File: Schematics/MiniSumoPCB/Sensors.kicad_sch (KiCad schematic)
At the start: 15 parts, among them J10 TOF_L, J11 TOF_R, J12 EXTRA_I2C1, J12 EXTRA_I2C2, J12 TOF_B, J7 Line_L, J7 TOF_F, J8 TOF_FR, J9 Line_R, J9 TOF_FL, U4 TCA9548APWR

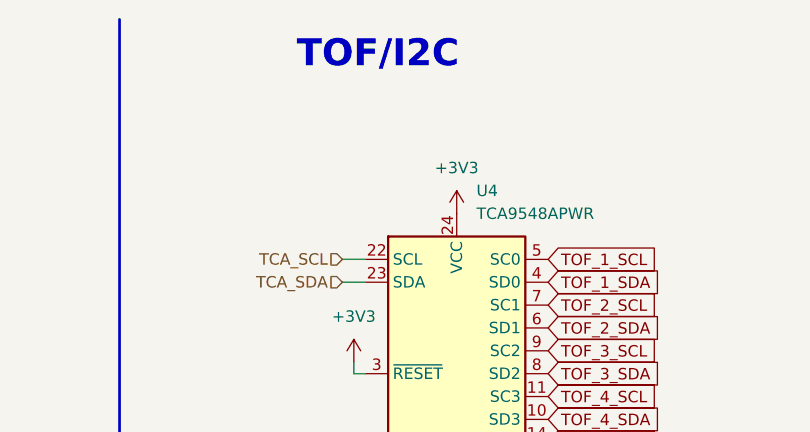
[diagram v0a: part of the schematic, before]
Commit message: [PCB] Added decoupling Capacitors
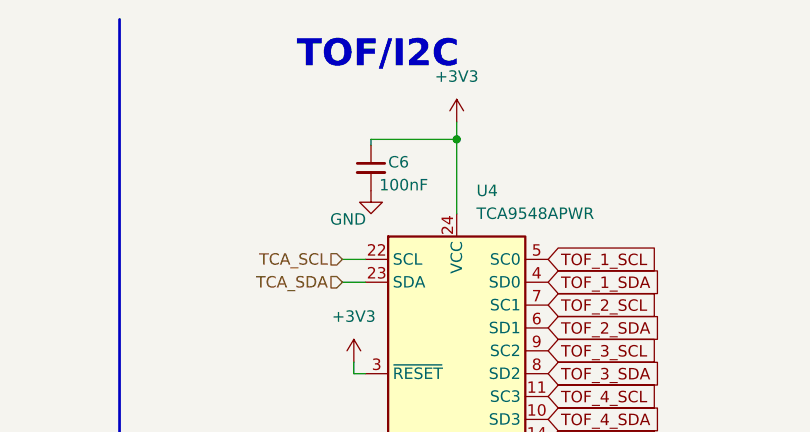
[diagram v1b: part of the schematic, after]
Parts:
- added C6: 100nF, Capacitor_SMD:C_1206_3216Metric_Pad1.33x1.80mm_HandSolder, symbol Device:C_Small
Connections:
- net +3V3: now also C6.1
- net GND: now also C6.2
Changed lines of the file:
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@@
   (junction (at 55.245 102.235) (diameter 0) (color 0 0 0 0)
   )
+  (junction (at 187.96 26.035) (diameter 0) (color 0 0 0 0)
+  )
   (wire (pts (xy 55.245 89.535) (xy 59.055 89.535))
     (stroke (width 0) (type default))
@@
     (stroke (width 0) (type default))
   )
+  (wire (pts (xy 178.435 26.67) (xy 178.435 26.035))
+    (stroke (width 0) (type default))
+  )
   (wire (pts (xy 176.53 69.85) (xy 176.53 72.39))
     (stroke (width 0) (type default))
@@
     (stroke (width 0) (type default))
   )
+  (wire (pts (xy 187.96 24.13) (xy 187.96 26.035))
+    (stroke (width 0) (type default))
+  )
   (wire (pts (xy 59.055 88.265) (xy 59.055 89.535))
     (stroke (width 0) (type default))
@@
     (stroke (width 0) (type default))
   )
+  (wire (pts (xy 178.435 26.035) (xy 187.96 26.035))
+    (stroke (width 0) (type default))
+  )
   (wire (pts (xy 243.205 64.77) (xy 244.475 64.77))
     (stroke (width 0) (type default))
@@
   )
   (polyline (pts (xy 150.495 197.485) (xy 151.13 197.485))
+    (stroke (width 0) (type default))
+  )
+  (wire (pts (xy 187.96 26.035) (xy 187.96 34.29))
     (stroke (width 0) (type default))
   )
@@
     )
   )
-  (symbol (lib_id "power:+3V3") (at 187.96 34.29 0) (mirror y) (unit 1)
-    (in_bom yes) (on_board yes) (dnp no) (fields_autoplaced)
-    (property "Reference" "#PWR023" (at 187.96 38.1 0)
-      (effects (font (size 1.27 1.27)) hide)
-    )
-    (property "Value" "+3V3" (at 187.96 29.21 0)
-      (effects (font (size 1.27 1.27)))
-    )
-    (property "Footprint" "" (at 187.96 34.29 0)
-      (effects (font (size 1.27 1.27)) hide)
-    )
-    (property "Datasheet" "" (at 187.96 34.29 0)
+  (symbol (lib_id "Device:C_Small") (at 178.435 29.21 0) (unit 1)
+    (in_bom yes) (on_board yes) (dnp no)
+    (property "Reference" "C6" (at 180.34 28.575 0)
+      (effects (font (size 1.27 1.27)) (justify left))
+    )
+    (property "Value" "100nF" (at 184.785 31.115 0)
+      (effects (font (size 1.27 1.27)) (justify right))
+    )
+    (property "Footprint" "Capacitor_SMD:C_1206_3216Metric_Pad1.33x1.80mm_HandSolder" (at 178.435 29.21 0)
+      (effects (font (size 1.27 1.27)) hide)
+    )
+    (property "Datasheet" "~" (at 178.435 29.21 0)
+      (effects (font (size 1.27 1.27)) hide)
+    )
+    (pin "1")
+    (pin "2")
+    (instances
+      (project "MiniSumoPCB"
+        (path "/0698a2d5-b2b6-4d73-8e30-63fb12402901"
+          (reference "C6") (unit 1)
+        )
+        (path "/0698a2d5-b2b6-4d73-8e30-63fb12402901/c2c084d3-faf8-46f3-8dc2-bbf086e8194e"
+          (reference "C11") (unit 1)
+        )
+      )
+      (project "SolarScavenger"
+        (path "/15d21b70-cf75-4246-a7d0-16607a291558"
+          (reference "C2") (unit 1)
+        )
+      )
+    )
+  )
+  (symbol (lib_id "power:+3V3") (at 187.96 24.13 0) (mirror y) (unit 1)
+    (in_bom yes) (on_board yes) (dnp no) (fields_autoplaced)
+    (property "Reference" "#PWR023" (at 187.96 27.94 0)
+      (effects (font (size 1.27 1.27)) hide)
+    )
+    (property "Value" "+3V3" (at 187.96 19.05 0)
+      (effects (font (size 1.27 1.27)))
+    )
+    (property "Footprint" "" (at 187.96 24.13 0)
+      (effects (font (size 1.27 1.27)) hide)
+    )
+    (property "Datasheet" "" (at 187.96 24.13 0)
       (effects (font (size 1.27 1.27)) hide)
     )
@@
         )
       )
+      (project "SolarScavenger"
+        (path "/15d21b70-cf75-4246-a7d0-16607a291558"
+          (reference "#PWR020") (unit 1)
+        )
+      )
+    )
+  )
+  (symbol (lib_id "power:GND") (at 178.435 31.75 0) (mirror y) (unit 1)
+    (in_bom yes) (on_board yes) (dnp no)
+    (property "Reference" "#PWR066" (at 178.435 38.1 0)
+      (effects (font (size 1.27 1.27)) hide)
+    )
+    (property "Value" "GND" (at 175.895 34.925 0)
+      (effects (font (size 1.27 1.27)))
+    )
+    (property "Footprint" "" (at 178.435 31.75 0)
+      (effects (font (size 1.27 1.27)) hide)
+    )
+    (property "Datasheet" "" (at 178.435 31.75 0)
+      (effects (font (size 1.27 1.27)) hide)
+    )
+    (pin "1")
+    (instances
+      (project "MiniSumoPCB"
+        (path "/0698a2d5-b2b6-4d73-8e30-63fb12402901"
+          (reference "#PWR066") (unit 1)
+        )
+        (path "/0698a2d5-b2b6-4d73-8e30-63fb12402901/c2c084d3-faf8-46f3-8dc2-bbf086e8194e"
+          (reference "#PWR068") (unit 1)
+        )
+      )

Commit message: Target tracking
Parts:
- R13, R16: value R -> 4k7
- R14, R17: value R -> 1k
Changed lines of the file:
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@@
   (symbol (lib_id "Device:R") (at 55.245 94.615 180) (unit 1)
     (in_bom yes) (on_board yes) (dnp no) (fields_autoplaced)
-    (property "Reference" "R16" (at 52.705 93.345 0)
-      (effects (font (size 1.27 1.27)) (justify left))
-    )
-    (property "Value" "R" (at 52.705 95.885 0)
+    (property "Reference" "R16" (at 53.34 93.345 0)
+      (effects (font (size 1.27 1.27)) (justify left))
+    )
+    (property "Value" "4k7" (at 53.34 95.885 0)
       (effects (font (size 1.27 1.27)) (justify left))
     )
@@
   (symbol (lib_id "Device:R") (at 55.245 55.245 180) (unit 1)
     (in_bom yes) (on_board yes) (dnp no) (fields_autoplaced)
-    (property "Reference" "R13" (at 52.705 53.975 0)
-      (effects (font (size 1.27 1.27)) (justify left))
-    )
-    (property "Value" "R" (at 52.705 56.515 0)
+    (property "Reference" "R13" (at 53.34 53.975 0)
+      (effects (font (size 1.27 1.27)) (justify left))
+    )
+    (property "Value" "4k7" (at 53.34 56.515 0)
       (effects (font (size 1.27 1.27)) (justify left))
     )
@@
   (symbol (lib_id "Device:R") (at 59.055 94.615 180) (unit 1)
     (in_bom yes) (on_board yes) (dnp no) (fields_autoplaced)
-    (property "Reference" "R17" (at 61.595 93.345 0)
+    (property "Reference" "R17" (at 60.96 93.345 0)
       (effects (font (size 1.27 1.27)) (justify right))
     )
-    (property "Value" "R" (at 61.595 95.885 0)
+    (property "Value" "1k" (at 60.96 95.885 0)
       (effects (font (size 1.27 1.27)) (justify right))
     )
@@
   (symbol (lib_id "Device:R") (at 59.055 55.245 180) (unit 1)
     (in_bom yes) (on_board yes) (dnp no) (fields_autoplaced)
-    (property "Reference" "R14" (at 61.595 53.975 0)
+    (property "Reference" "R14" (at 60.96 53.975 0)
       (effects (font (size 1.27 1.27)) (justify right))
     )
-    (property "Value" "R" (at 61.595 56.515 0)
+    (property "Value" "1k" (at 60.96 56.515 0)
       (effects (font (size 1.27 1.27)) (justify right))
     )

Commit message: Update Readme.md
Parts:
- renumbered C6 to C11, J7 to J10, J8 to J11, J9 to J12, J10 to J13, J11 to J14, J12 to J15, J12 to J16, J12 to J17
